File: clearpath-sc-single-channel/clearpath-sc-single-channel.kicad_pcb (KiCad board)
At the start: 2 copper layers, 75 x 50 mm, 53 parts, among them P1 MOLEX_MICROFIT_JR_RH_2x1_WAY, P2 MOLEX_MICROFIT_JR_RH_2x2_WAY, P3 MOLEX_MICROFIT_JR_RH_2x2_WAY, P4 MOLEX_MICROFIT_JR_RH_2x4_WAY, Q1 MMBT5401, Q2 MMBTA06, U1 LM317LCPK, U2 FT230XS-R, U3 USBLC6, U4 LM317LCPK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

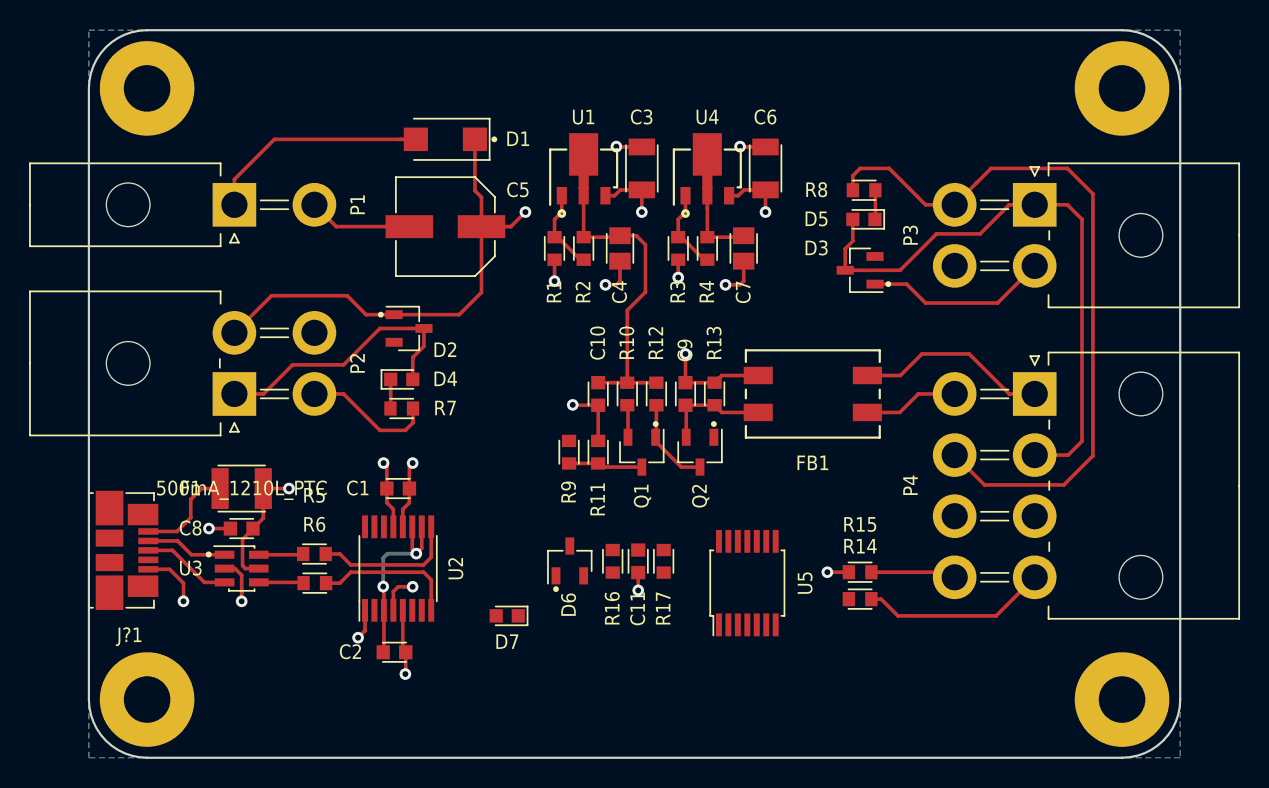
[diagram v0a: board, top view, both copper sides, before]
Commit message: Reworked hex inverter and finished routing
Increased trace thickness, all drc errors removed, improved hex schmitt wiring by shuffling unit allocation in schematic.
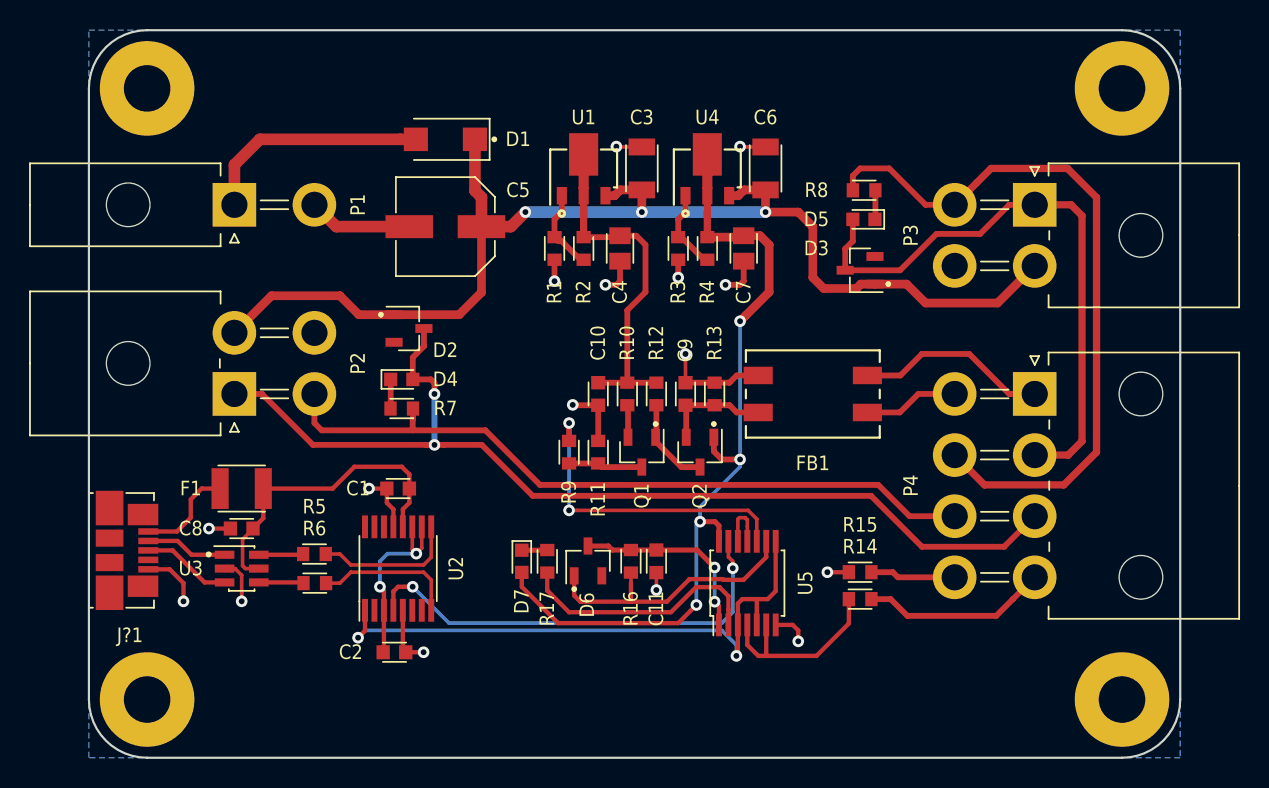
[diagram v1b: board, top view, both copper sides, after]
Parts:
- moved R17 8.00 mm to (131.5, 136.5), turned to 270 degrees
- moved D7 3.88 mm to (129.8, 136.5), turned to 270 degrees
- moved C11 1.25 mm to (139.0, 136.5)
- moved D6 1.25 mm to (134.3, 136.5)
- moved R16 1.25 mm to (137.2, 136.5)
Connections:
- U5 pad 1: Net-(R9-Pad2) -> Net-(C11-Pad1)
- U5 pad 10: SERIAL_TX -> Net-(R9-Pad2)
- U5 pad 11: Net-(D6-Pad1) -> Net-(U5-Pad11)
- U5 pad 12: Net-(C11-Pad1) -> Net-(U5-Pad11)
- U5 pad 13: Net-(R17-Pad2) -> SERIAL_RX
- U5 pad 2: Net-(U5-Pad2) -> Net-(R17-Pad2)
- U5 pad 3: Net-(U5-Pad2) -> SERIAL_TX
- U5 pad 4: SERIAL_RX -> Net-(R14-Pad2)
- U5 pad 9: Net-(R14-Pad2) -> Net-(D6-Pad1)
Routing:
- net +5V: track 5.39 -> 57.1 mm, vias 0 -> 4
- net INPUT_A+: track 18.7 -> 69.9 mm, vias 0 -> 2
- net INPUT_A-: track 9.00 -> 50.2 mm
- net SERIAL_TX: track 2.08 -> 41.2 mm, vias 1 -> 2
- net +POWER: track 54.3 -> 82.7 mm
- net SERIAL_RX: track 2.75 -> 31.1 mm, vias 1 -> 2
- net Net-(R9-Pad2): track 0.00 -> 21.9 mm, vias 0 -> 2
- net Net-(D6-Pad1): track 0.00 -> 19.1 mm
- net Net-(R17-Pad2): track 0.00 -> 17.2 mm
- net Net-(R14-Pad2): track 0.00 -> 13.4 mm
- net Net-(C11-Pad1): track 0.00 -> 13.4 mm, vias 0 -> 2
- net USB_VDD: track 13.5 -> 21.8 mm, vias 2 -> 0
- net Net-(U5-Pad11): track 0.00 -> 3.76 mm
- net +12V: track 21.4 -> 24.2 mm
- net Net-(D7-PadC): track 0.00 -> 1.76 mm
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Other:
- rule trace_min: 0.25 -> 0.22
- board text added: "PCB Stackup Preferences 2 Layer, 1.6mm FR4 1oz copper on top & bottom Green Soldermask with ENIG Min Track: 0.25mm Min Via Drill: 0.4mm"
- board text removed: "PCB Stackup Preferences 2 Layer, 1.6mm FR4 1oz copper on top & bottom Green Soldermask with ENIG Min Track: 0.3mm Min Via Drill: 0.4mm"

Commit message: Cosmetic improvements
Added silkscreen text and voltage test points
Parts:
- added TEST1: CLIP_HOOK_RED, Applidyne_Test:KEYSTONE_5000, F.Cu at (132.0, 105.8)
- added TEST2: CLIP_HOOK_RED, Applidyne_Test:KEYSTONE_5000, F.Cu at (140.5, 105.8)
- added TEST3: CLIP_HOOK_BLACK, Applidyne_Test:KEYSTONE_5001, F.Cu at (150.8, 105.8)
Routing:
- net +12V: track 24.2 -> 28.7 mm
- net +5V: track 57.1 -> 61.2 mm
- net Net-(D6-Pad1): track 19.1 -> 19.7 mm
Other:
- board text added: "12-24V"
- board text added: "12V"
- board text added: "5V"
- board text added: "CLEARPATH-SC1"
- board text added: "DATA"
- board text added: "GND"
- board text added: "INPUT_A"
- board text added: "INPUT_B"
- board text added: "POWER"
